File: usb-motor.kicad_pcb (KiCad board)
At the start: 4 copper layers, 78.7 x 68.6 mm, 252 parts, among them J1 BATT, J10 Power, J11 USB_C_Receptacle, J12 I2Cx, J13 xpins, J14 CHG_CTL, J15 VBUS, J16 Events, J17 VBUS, J18 i2c, J19 CHG_CTL, J2 Cells, J20 VSYS, J21 PWR, J22 Motor controls, J23 3v3, J24 I2C, J3 Cells, J4 Motor, J5 EVENTS, J6 VSYS, J7 I2C, J8 PWR, J9 Motor controls, Q1 CSD87333Q3D, Q2 CSD87333Q3D, Q3 FDMA6676PZ, Q4 FDN358P, Q5 CSD87313DMS, Q6 CSD87503Q3E, Q7 CSD87503Q3E, SW1 WAKE/PWR, SW2 RESET, U1 BQ25713(B), U10 TPD6S300A, U11 SWD, U12 CYPD3123-40LQXIT, U2 CSD15380F3, U3 CSD15380F3, U4 BQ4050R, U5 IFX9201SG, U6 SN74LVC1G14DPWR, U7 SN74LVC1G08DPWR, U8 BNX02x, U9 LMZM23601V3

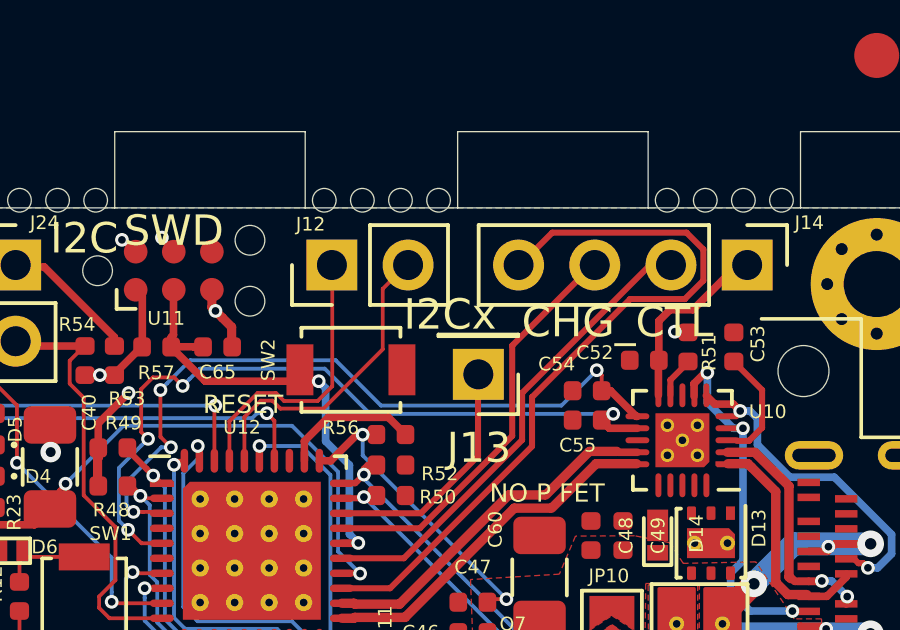
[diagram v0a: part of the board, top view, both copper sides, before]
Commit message: Post fab edits for assembly
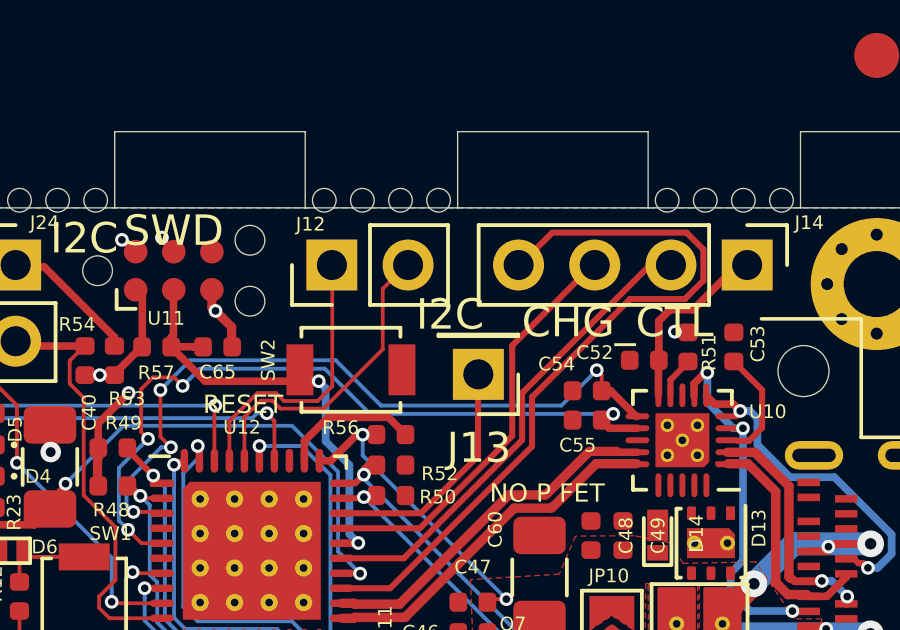
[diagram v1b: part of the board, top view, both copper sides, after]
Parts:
- C31, C32, C45: value >22uF -> 22uF
- C38: value 0.1F -> 0.1uF
- C50: value 10uF 25V+ -> 10uF
- C53: value 0.1uF 50V X7R -> 0.1uF
- FID1, FID2, FID3: renamed from REF**; value Fiducial_1.5mm_Mask3mm -> Fiducial
- J12: value I2Cx -> I2C
- MOU1, MOU10, MOU11, MOU12, MOU13, MOU14, MOU15, MOU16, MOU17, MOU18, MOU19, MOU2, MOU20, MOU21, MOU22, MOU23, MOU24, MOU25, MOU26, MOU27, MOU28, MOU29, MOU3, MOU30, MOU31, MOU32, MOU4, MOU5, MOU6, MOU7, MOU8, MOU9: renamed from REF**; value mousebites -> Mousebite
- R22, R7: value 0.01 -> 10m
- R26, R27, R3: value 10k -> 10.0k
- R48, R49, R50, R52: value 10M -> 10.0M
- R55: value 10m 1% -> 10m
- U6: value SN74LVC1G14DPWR -> SN74LVC1G14D
- U7: value SN74LVC1G08DPWR -> SN74LVC1G08D
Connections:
- net /BATT renamed /6-36V
- J11 pad A10: (no net) -> Net-(J11-PadA10)
- J11 pad A11: (no net) -> Net-(J11-PadA11)
- J11 pad A2: (no net) -> Net-(J11-PadA2)
- J11 pad A3: (no net) -> Net-(J11-PadA3)
- J11 pad A8: (no net) -> Net-(J11-PadA8)
- J11 pad B10: (no net) -> Net-(J11-PadB10)
- J11 pad B11: (no net) -> Net-(J11-PadB11)
- J11 pad B2: (no net) -> Net-(J11-PadB2)
- J11 pad B3: (no net) -> Net-(J11-PadB3)
- J11 pad B8: (no net) -> Net-(J11-PadB8)
- Q1 pad 4: (no net) -> Net-(Q1-Pad4)
- Q2 pad 4: (no net) -> Net-(Q2-Pad4)
- U1 pad 15: (no net) -> Net-(U1-Pad15)
- U10 pad 16: (no net) -> Net-(U10-Pad16)
- U10 pad 17: (no net) -> Net-(U10-Pad17)
- U10 pad 19: (no net) -> Net-(U10-Pad19)
- U10 pad 20: (no net) -> Net-(U10-Pad20)
- U11 pad 6: (no net) -> Net-(U11-Pad6)
- U12 pad 4: (no net) -> /5V
- U12 pad 6: (no net) -> Net-(U12-Pad6)
- U4 pad 15: (no net) -> Net-(U4-Pad15)
- U9 pad 10: (no net) -> Net-(U9-Pad10)
- U9 pad 5: (no net) -> Net-(U9-Pad5)
- U9 pad 8: (no net) -> Net-(U9-Pad8)
- U9 pad 9: (no net) -> Net-(U9-Pad9)

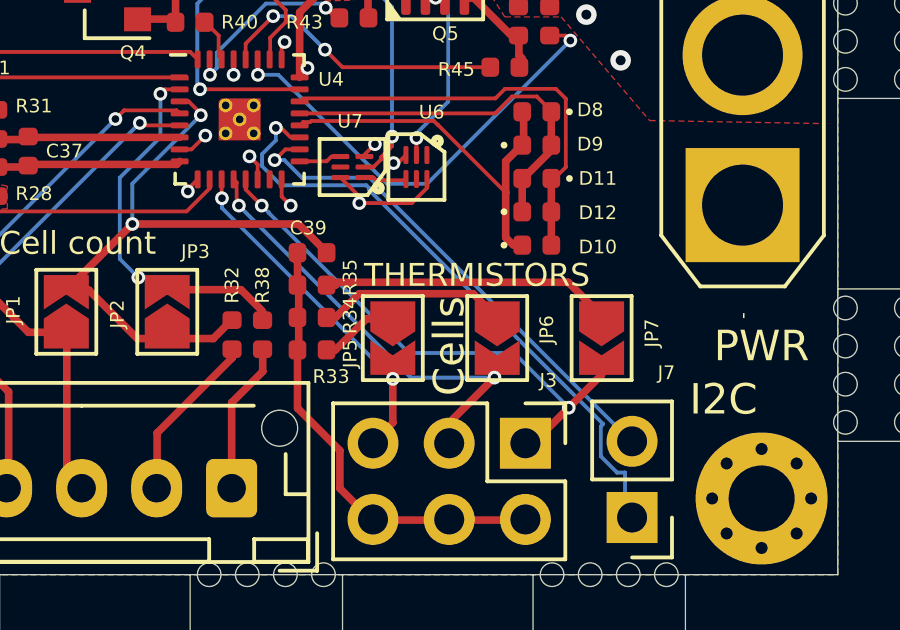
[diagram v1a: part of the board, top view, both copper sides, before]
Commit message: fix cells dup name
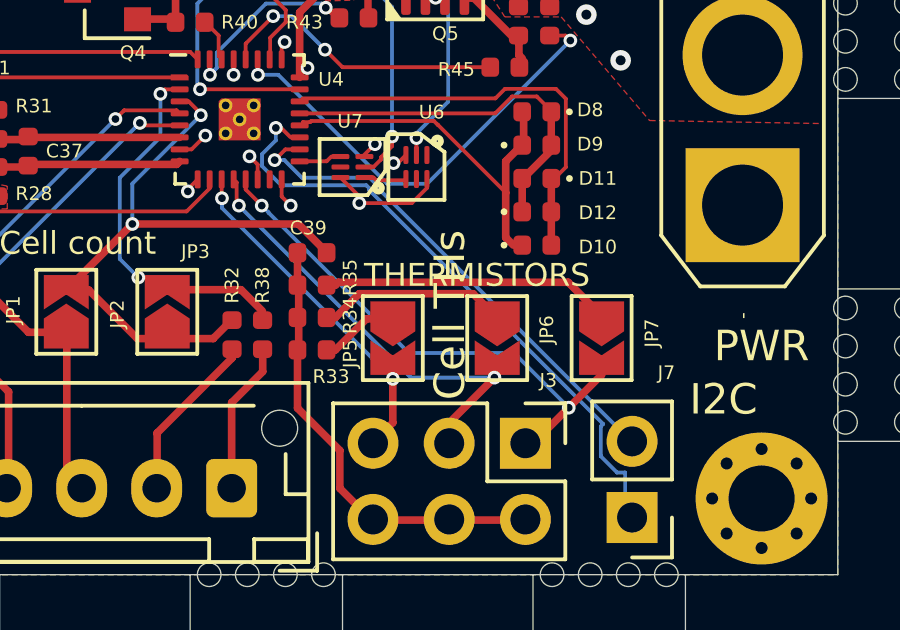
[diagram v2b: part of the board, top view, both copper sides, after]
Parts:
- C61: value 1uF X7R -> 1uF
- J3: value Cells -> Cell THs
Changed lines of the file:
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@@
       (effects (font (size 0.4572 0.4572) (thickness 0.0762)))
     )
-    (fp_text value "Cells" (at -3.2385 2.54 90) (layer "F.SilkS")
+    (fp_text value "Cell THs" (at -4.27482 2.51714 90) (layer "F.SilkS")
       (effects (font (size 1.016 1.016) (thickness 0.1524)))
     )
@@
       (effects (font (size 0.4572 0.4572) (thickness 0.0762)))
     )
-    (fp_text value "1uF X7R" (at 0 1.17) (layer "F.Fab")
-      (effects (font (size 1.016 1.016) (thickness 0.1524)))
-    )
+    (fp_text value "1uF" (at 0 1.17) (layer "F.Fab")
+      (effects (font (size 1.016 1.016) (thickness 0.1524)))
+    )

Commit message: post fab error fixes, brushed motor needs refabbed.
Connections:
- U5 pad 13: /Brushed 12V Motor/GNDF -> (no net)
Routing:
- net /PWM: track 34.7 -> 36.1 mm
- net /SI: track 46.2 -> 47.5 mm
- net /VDDD: track 124.5 -> 125.3 mm
- net /DIS: track 59.5 -> 60.0 mm
- net /Brushed 12V Motor/GNDF: track 2.06 -> 1.89 mm, vias 17 -> 18
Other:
- board text added: "USB Motor Fyber Labs Inc. 2019 0.3.0-b Brushed Motor"
- board text removed: "USB Motor Fyber Labs Inc. 2019 0.3.0-a Brushed Motor"
